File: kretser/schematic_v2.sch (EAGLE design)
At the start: 18 parts, among them IC1 ATMEGA168-20PU, U2 LM2940CT-5.0/NOPB

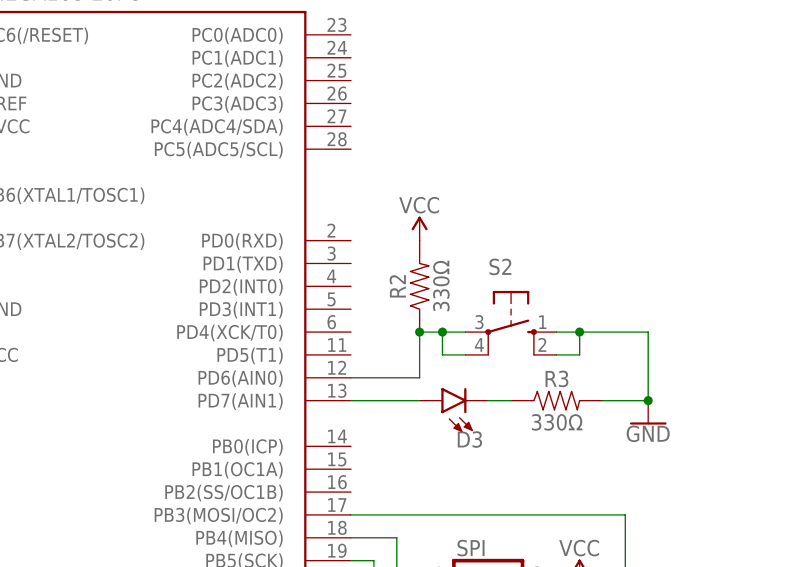
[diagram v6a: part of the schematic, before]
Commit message: Fixed switch connection pin 12
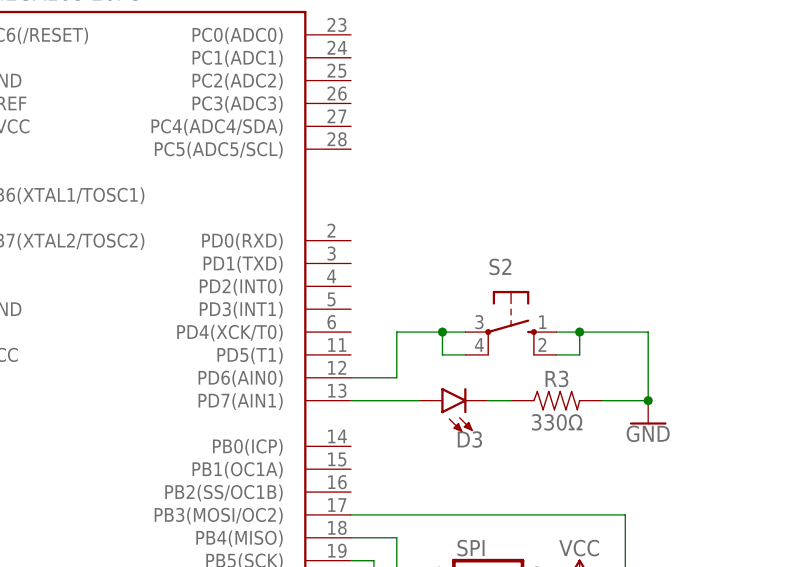
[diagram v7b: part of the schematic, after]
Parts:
- removed R2: 330Ω, SparkFun-Resistors:10OHM-HORIZ-1/4W-1%
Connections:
- net N$8: no longer R2.1
- net VCC: no longer R2.2
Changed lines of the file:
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@@
 <part name="C5" library="SparkFun-Capacitors" library_urn="urn:adsk.eagle:library:510" deviceset="470PF" device="-0603-50V-5%" package3d_urn="urn:adsk.eagle:package:41385090/1" value="100nF"/>
 <part name="SUPPLY5" library="SparkFun-PowerSymbols" library_urn="urn:adsk.eagle:library:530" deviceset="VCC" device="" value="VCC"/>
-<part name="SUPPLY2" library="SparkFun-PowerSymbols" library_urn="urn:adsk.eagle:library:530" deviceset="VCC" device="" value="VCC"/>
 <part name="SUPPLY6" library="SparkFun-PowerSymbols" library_urn="urn:adsk.eagle:library:530" deviceset="VCC" device="" value="VCC"/>
 <part name="GND4" library="SparkFun-PowerSymbols" library_urn="urn:adsk.eagle:library:530" deviceset="GND" device=""/>
@@
 <part name="SUPPLY4" library="SparkFun-PowerSymbols" library_urn="urn:adsk.eagle:library:530" deviceset="VCC" device="" value="VCC"/>
 <part name="R1" library="SparkFun-Resistors" library_urn="urn:adsk.eagle:library:532" deviceset="10OHM" device="-HORIZ-1/4W-1%" package3d_urn="urn:adsk.eagle:package:39658/2" value="330Ω"/>
-<part name="R2" library="SparkFun-Resistors" library_urn="urn:adsk.eagle:library:532" deviceset="10OHM" device="-HORIZ-1/4W-1%" package3d_urn="urn:adsk.eagle:package:39658/2" value="330Ω"/>
 </parts>
 <sheets>
@@
 <attribute name="VALUE" x="68.58" y="134.366" size="1.778" layer="96" font="vector" rot="R180" align="bottom-center"/>
 </instance>
-<instance part="SUPPLY2" gate="G$1" x="152.4" y="91.44" smashed="yes">
-<attribute name="VALUE" x="152.4" y="96.266" size="1.778" layer="96" font="vector" rot="R180" align="bottom-center"/>
-</instance>
 <instance part="SUPPLY6" gate="G$1" x="170.18" y="53.34" smashed="yes">
 <attribute name="VALUE" x="170.18" y="58.166" size="1.778" layer="96" font="vector" rot="R180" align="bottom-center"/>
@@
 <attribute name="NAME" x="39.116" y="109.22" size="1.778" layer="95" font="vector" rot="R90" align="bottom-center"/>
 <attribute name="VALUE" x="42.164" y="109.22" size="1.778" layer="96" font="vector" rot="R90" align="top-center"/>
-</instance>
-<instance part="R2" gate="G$1" x="152.4" y="86.36" smashed="yes" rot="R90">
-<attribute name="NAME" x="150.876" y="86.36" size="1.778" layer="95" font="vector" rot="R90" align="bottom-center"/>
-<attribute name="VALUE" x="153.924" y="86.36" size="1.778" layer="96" font="vector" rot="R90" align="top-center"/>
 </instance>
 </instances>
@@
 <junction x="93.98" y="76.2"/>
 </segment>
-<segment>
-<pinref part="R2" gate="G$1" pin="2"/>
-<pinref part="SUPPLY2" gate="G$1" pin="VCC"/>
-</segment>
 </net>
 <net name="N$5" class="0">
@@
 <wire x1="154.94" y1="78.74" x2="154.94" y2="81.28" width="0.1524" layer="91"/>
 <pinref part="IC1" gate="G$1" pin="PD6(AIN0)"/>
-<wire x1="144.78" y1="76.2" x2="152.4" y2="76.2" width="0.1524" layer="91"/>
-<wire x1="154.94" y1="81.28" x2="152.4" y2="81.28" width="0.1524" layer="91"/>
-<wire x1="152.4" y1="81.28" x2="152.4" y2="76.2" width="0.1524" layer="91"/>
+<wire x1="144.78" y1="76.2" x2="149.86" y2="76.2" width="0.1524" layer="91"/>
+<wire x1="149.86" y1="76.2" x2="149.86" y2="81.28" width="0.1524" layer="91"/>
+<wire x1="149.86" y1="81.28" x2="154.94" y2="81.28" width="0.1524" layer="91"/>
 <junction x="154.94" y="81.28"/>
-<pinref part="R2" gate="G$1" pin="1"/>
-<junction x="152.4" y="81.28"/>
-</segment>
-</net>
+</segment>
+</net>

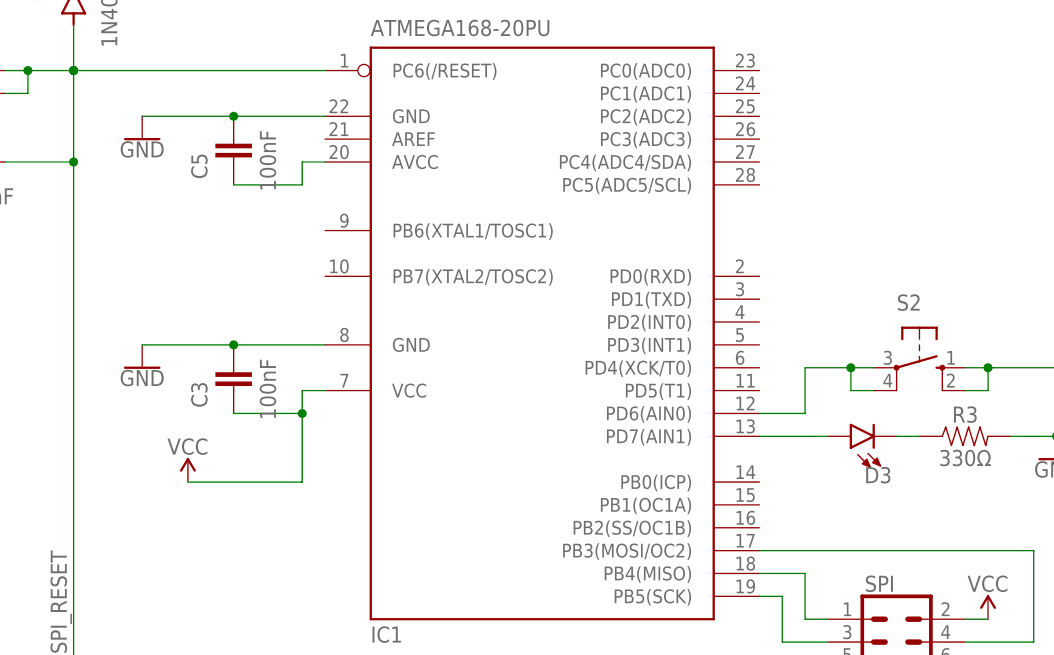
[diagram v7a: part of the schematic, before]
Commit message: Connected AVCC to VCC.
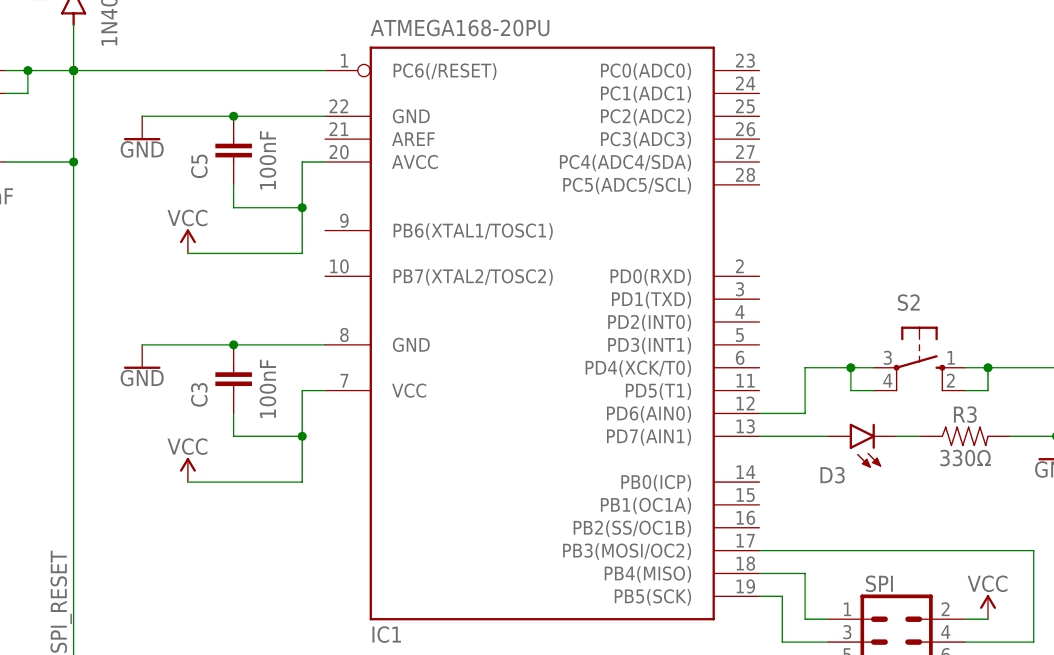
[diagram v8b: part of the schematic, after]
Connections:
- removed net N$5: C5.1, IC1.AVCC
- net VCC: now also C5.1, IC1.AVCC
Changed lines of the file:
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@@
 <part name="SUPPLY4" library="SparkFun-PowerSymbols" library_urn="urn:adsk.eagle:library:530" deviceset="VCC" device="" value="VCC"/>
 <part name="R1" library="SparkFun-Resistors" library_urn="urn:adsk.eagle:library:532" deviceset="10OHM" device="-HORIZ-1/4W-1%" package3d_urn="urn:adsk.eagle:package:39658/2" value="330Ω"/>
+<part name="SUPPLY2" library="SparkFun-PowerSymbols" library_urn="urn:adsk.eagle:library:530" deviceset="VCC" device="" value="VCC"/>
 </parts>
 <sheets>
@@
 </instance>
 <instance part="D3" gate="D1" x="154.94" y="73.66" smashed="yes" rot="R90">
-<attribute name="NAME" x="159.512" y="70.231" size="1.778" layer="95" font="vector" rot="R180"/>
+<attribute name="NAME" x="154.432" y="70.231" size="1.778" layer="95" font="vector" rot="R180"/>
 <attribute name="VALUE" x="159.512" y="75.565" size="1.778" layer="96" font="vector" rot="R180" align="top-left"/>
 </instance>
@@
 <attribute name="NAME" x="39.116" y="109.22" size="1.778" layer="95" font="vector" rot="R90" align="bottom-center"/>
 <attribute name="VALUE" x="42.164" y="109.22" size="1.778" layer="96" font="vector" rot="R90" align="top-center"/>
+</instance>
+<instance part="SUPPLY2" gate="G$1" x="81.28" y="93.98" smashed="yes">
+<attribute name="VALUE" x="81.28" y="98.806" size="1.778" layer="96" font="vector" rot="R180" align="bottom-center"/>
 </instance>
 </instances>
@@
 <pinref part="IC1" gate="G$1" pin="VCC@1"/>
 <wire x1="96.52" y1="78.74" x2="93.98" y2="78.74" width="0.1524" layer="91"/>
-<wire x1="93.98" y1="78.74" x2="93.98" y2="76.2" width="0.1524" layer="91"/>
+<wire x1="81.28" y1="68.58" x2="93.98" y2="68.58" width="0.1524" layer="91"/>
+<wire x1="93.98" y1="68.58" x2="93.98" y2="73.66" width="0.1524" layer="91"/>
 <pinref part="C3" gate="G$1" pin="1"/>
-<wire x1="93.98" y1="76.2" x2="86.36" y2="76.2" width="0.1524" layer="91"/>
-<wire x1="81.28" y1="68.58" x2="93.98" y2="68.58" width="0.1524" layer="91"/>
-<wire x1="93.98" y1="68.58" x2="93.98" y2="76.2" width="0.1524" layer="91"/>
-<junction x="93.98" y="76.2"/>
-</segment>
-</net>
-<net name="N$5" class="0">
-<segment>
-<pinref part="C5" gate="G$1" pin="1"/>
+<wire x1="93.98" y1="73.66" x2="93.98" y2="78.74" width="0.1524" layer="91"/>
+<wire x1="86.36" y1="76.2" x2="86.36" y2="73.66" width="0.1524" layer="91"/>
+<wire x1="86.36" y1="73.66" x2="93.98" y2="73.66" width="0.1524" layer="91"/>
+<junction x="93.98" y="73.66"/>
+</segment>
+<segment>
 <pinref part="IC1" gate="G$1" pin="AVCC"/>
 <wire x1="96.52" y1="104.14" x2="93.98" y2="104.14" width="0.1524" layer="91"/>
-<wire x1="93.98" y1="104.14" x2="93.98" y2="101.6" width="0.1524" layer="91"/>
-<wire x1="93.98" y1="101.6" x2="86.36" y2="101.6" width="0.1524" layer="91"/>
-</segment>
-</net>
+<pinref part="SUPPLY2" gate="G$1" pin="VCC"/>
+<wire x1="81.28" y1="93.98" x2="93.98" y2="93.98" width="0.1524" layer="91"/>
+<wire x1="93.98" y1="93.98" x2="93.98" y2="99.06" width="0.1524" layer="91"/>
+<pinref part="C5" gate="G$1" pin="1"/>
+<wire x1="93.98" y1="99.06" x2="93.98" y2="104.14" width="0.1524" layer="91"/>
+<wire x1="86.36" y1="101.6" x2="86.36" y2="99.06" width="0.1524" layer="91"/>
+<wire x1="86.36" y1="99.06" x2="93.98" y2="99.06" width="0.1524" layer="91"/>
+<junction x="93.98" y="99.06"/>
+</segment>
+</net>
